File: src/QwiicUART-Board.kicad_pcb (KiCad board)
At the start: 2 copper layers, 25.4 x 25.4 mm, 19 parts, among them J1 QWIIC, J2 QWIIC, J3 FTDI, U1 SC16IS741A, X1 ECS-2520MVLC-018-BN-TR

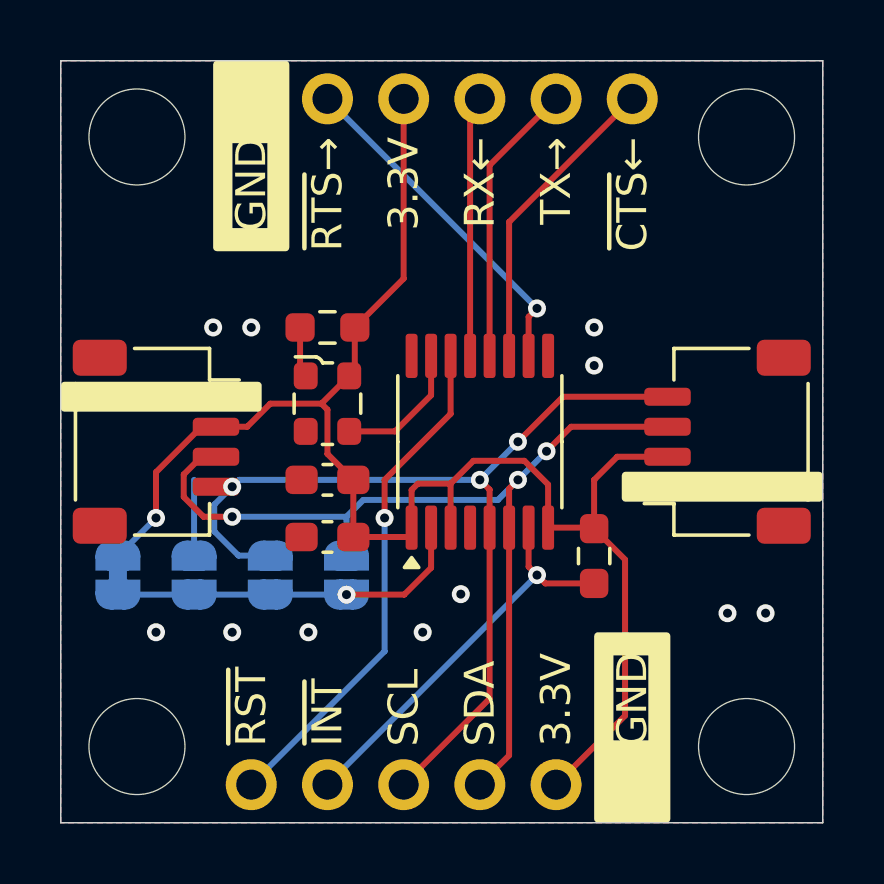
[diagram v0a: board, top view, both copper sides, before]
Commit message: Changed repository name. Changed address numbers on back of board. Added a test point for the clock.
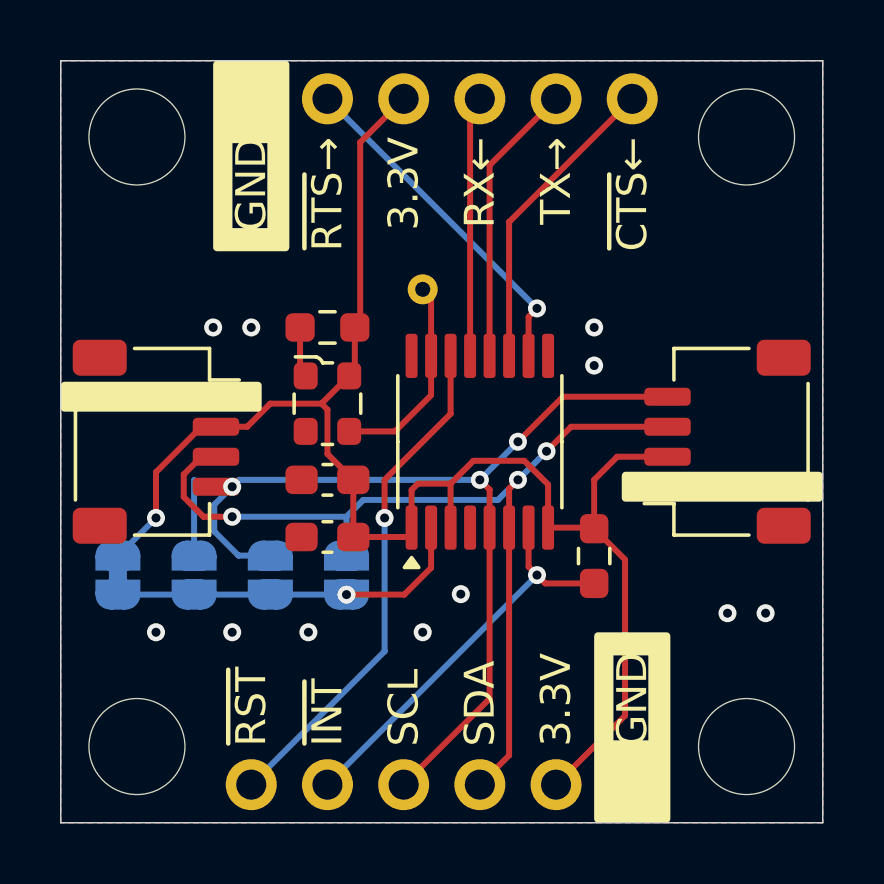
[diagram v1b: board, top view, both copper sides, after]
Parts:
- added TP1: TestPoint, TestPoint:TestPoint_THTPad_D1.0mm_Drill0.5mm, F.Cu at (139.1, 102.9)
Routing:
- net /CLK: track 4.54 -> 6.88 mm
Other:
- board text added: "0x48"
- board text added: "0x49"
- board text added: "0x4A"
- board text added: "0x4B"
- board text removed: "0x90"
- board text removed: "0x92"
- board text removed: "0x94"
- board text removed: "0x96"
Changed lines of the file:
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@@
 	(paper "USLetter")
 	(title_block
-		(title "Qwiic UART")
-		(date "2025-01-11")
-		(rev "0.0.1")
+		(title "Qwiic UART Board")
+		(date "2025-02-08")
+		(rev "0.0.2")
 		(company "Designer: C. M. Bulliner")
 		(comment 2 "OF MERCHANTABILITY, SATISFACTORY QUALITY AND FITNESS FOR A PARTICULAR PURPOSE.")
@@
 		(grid_origin 139.7 107.95)
 		(pcbplotparams
-			(layerselection 0x00010fc_ffffffff)
+			(layerselection 0x00010f8_ffffffff)
 			(plot_on_all_layers_selection 0x0000000_00000000)
 			(disableapertmacros no)
@@
 		)
 	)
+	(footprint "TestPoint:TestPoint_THTPad_D1.0mm_Drill0.5mm"
+		(layer "F.Cu")
+		(at 139.065 102.87)
+		(descr "THT pad as test Point, diameter 1.0mm, hole diameter 0.5mm")
+		(tags "test point THT pad")
+		(property "Reference" "TP1"
+			(at 0 -1.448 0)
+			(layer "F.SilkS")
+			(hide yes)
+			(effects
+				(font
+					(size 1 1)
+					(thickness 0.15)
+				)
+			)
+		)
+		(property "Value" "TestPoint"
+			(at 0 1.55 0)
+			(layer "F.Fab")
+			(hide yes)
+			(effects
+				(font
+					(size 1 1)
+					(thickness 0.15)
+				)
+			)
+		)
+		(property "Footprint" "TestPoint:TestPoint_THTPad_D1.0mm_Drill0.5mm"
+			(at 0 0 0)
+			(unlocked yes)
+			(layer "F.Fab")
+			(hide yes)
+			(effects
+				(font
+					(size 1.27 1.27)
+					(thickness 0.15)
+				)
+			)
+		)
+		(property "Datasheet" ""
+			(at 0 0 0)
+			(unlocked yes)
+			(layer "F.Fab")
+			(hide yes)
+			(effects
+				(font
+					(size 1.27 1.27)
+					(thickness 0.15)
+				)
+			)
+		)
+		(property "Description" "test point"
+			(at 0 0 0)
+			(unlocked yes)
+			(layer "F.Fab")
+			(hide yes)
+			(effects
+				(font
+					(size 1.27 1.27)
+					(thickness 0.15)
+				)
+			)
+		)
+		(property ki_fp_filters "Pin* Test*")
+		(sheetname "Root")
+		(sheetfile "Qwiic-UART.kicad_sch")
+		(attr exclude_from_pos_files)
+		(fp_circle
+			(center 0 0)
+			(end 1 0)
+			(stroke
+				(width 0.05)
+				(type solid)
+			)
+			(fill none)
+			(layer "F.CrtYd")
+		)
+		(fp_text user "${REFERENCE}"
+			(at 0 -1.45 0)
+			(layer "F.Fab")
+			(hide yes)
+			(effects
+				(font
+					(size 1 1)
+					(thickness 0.15)
+				)
+			)
+		)
+		(pad "1" thru_hole circle
+			(at 0 0)
+			(size 1 1)
+			(drill 0.5)
+			(layers "*.Cu" "*.Mask")
+			(remove_unused_layers no)
+			(net 19 "/CLK")
+			(pinfunction "1")
+			(pintype "passive")
+		)
+	)
 	(footprint "Connector_JST:JST_SH_SM04B-SRSS-TB_1x04-1MP_P1.00mm_Horizontal"
 		(layer "F.Cu")
@@
 		)
 	)
-	(gr_text "0x90"
-		(at 128.905 110.49 -90)
+	(gr_text "0x48"
+		(at 128.905 110.49 270)
 		(layer "B.SilkS")
 		(effects
@@
 		)
 	)
-	(gr_text "0x92"
-		(at 131.445 110.49 -90)
+	(gr_text "0x49"
+		(at 131.445 110.49 270)
 		(layer "B.SilkS")
 		(effects
@@
 		)
 	)
-	(gr_text "0x94"
-		(at 133.985 110.49 -90)
+	(gr_text "0x4A"
+		(at 133.985 110.49 270)
 		(layer "B.SilkS")
 		(effects
@@
 		)
 	)
-	(gr_text "0x96"
+	(gr_text "0x4B"
 		(at 136.525 110.49 270)
 		(layer "B.SilkS")
@@
 		)
 	)
-	(gr_text "Circuit Board Specifications\n\nBoard Thickness: 1.6 mm\nSubstrate Material: FR4\nCopper Layers: 2\nCopper Thickness: 1 oz\nSoldermask Color: Any (Blue Suggested)\nSurface Finish: Any (HASL Lead-Free Suggested)\n\nSmallest Hole Diameter: 0.3 mm [11.8 mil]\nSmallest Trace Width: 0.2 mm [7.8 mil]\nSmallest Trace Spacing: 0.2 mm [7.8 mil]\n\nDocumentation and source files can be found at\nhttps://github.com/CMB27/Qwiic-UART."
+	(gr_text "Circuit Board Specifications\n\nBoard Thickness: 1.6 mm\nSubstrate Material: FR4\nCopper Layers: 2\nCopper Thickness: 1 oz\nSoldermask Color: Any (Blue Suggested)\nSurface Finish: Any (HASL Lead-Free Suggested)\n\nSmallest Hole Diameter: 0.3 mm [11.8 mil]\nSmallest Trace Width: 0.2 mm [7.8 mil]\nSmallest Trace Spacing: 0.2 mm [7.8 mil]\n\nDocumentation and source files can be found at\nhttps://github.com/CMB27/QwiicUART-Board."
 		(at 15.24 200.66 0)
 		(layer "Cmts.User")
@@
 	)
 	(segment
-		(start 136.8025 104.14)
-		(end 138.43 102.5125)
-		(width 0.2)
-		(layer "F.Cu")
-		(net 2)
-	)
-	(segment
 		(start 140.756471 108.585)
 		(end 142.45353 108.585)
@@
 	)
 	(segment
-		(start 138.43 102.5125)
-		(end 138.43 96.52)
+		(start 136.98125 103.96125)
+		(end 136.98125 97.96875)
 		(width 0.2)
 		(layer "F.Cu")
@@
 	)
 	(segment
+		(start 136.98125 97.96875)
+		(end 138.43 96.52)
+		(width 0.2)
+		(layer "F.Cu")
+		(net 2)
+	)
+	(segment
 		(start 143.245 110.8125)
 		(end 144.745 110.8125)
@@
 	)
 	(segment
+		(start 136.8025 104.14)
+		(end 136.98125 103.96125)
+		(width 0.2)
+		(layer "F.Cu")
+		(net 2)
+	)
+	(segment
 		(start 135.89 106.88)
 		(end 135.69 106.68)
@@
 	)
 	(segment
+		(start 139.345 105.0875)
+		(end 139.345 103.15)
+		(width 0.2)
+		(layer "F.Cu")
+		(net 19)
+	)
+	(segment
 		(start 136.615 107.605)
 		(end 138.14 107.605)
@@
 		(width 0.2)
 		(layer "F.Cu")
+		(net 19)
+	)
+	(segment
+		(start 139.345 103.15)
+		(end 139.065 102.87)
+		(width 0.2)
+		(layer "F.Cu")
